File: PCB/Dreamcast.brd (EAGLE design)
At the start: 58.5 x 61 mm, 17 parts

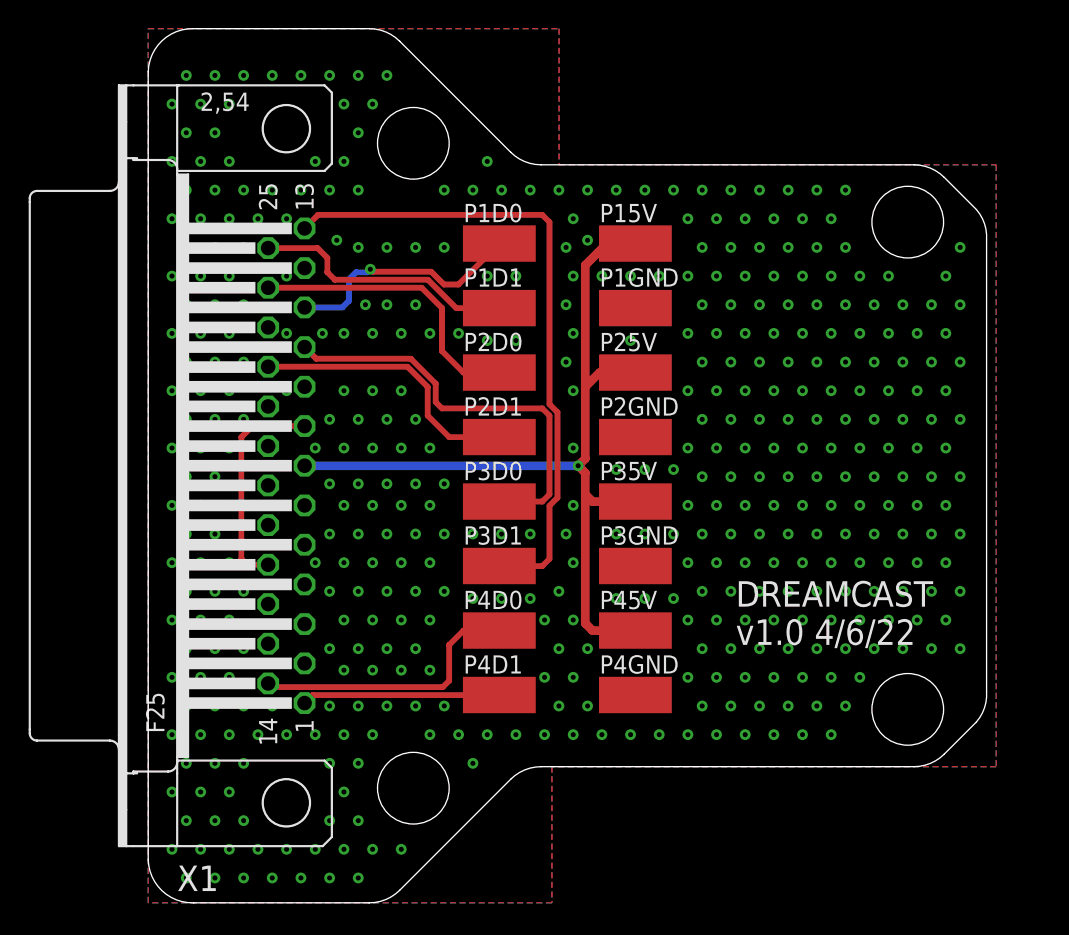
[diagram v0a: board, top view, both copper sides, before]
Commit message: Updates from Issues 42/43/18
Closed Issues 42 and 43 as Sega Genesis and PSX have been successfully tested and functional.

Updated Dreamcast PCB per comment in Issue 18 - Reversed P1-P4 pads to match housing

Updated Project Status to reflect #42 and #43 Complete
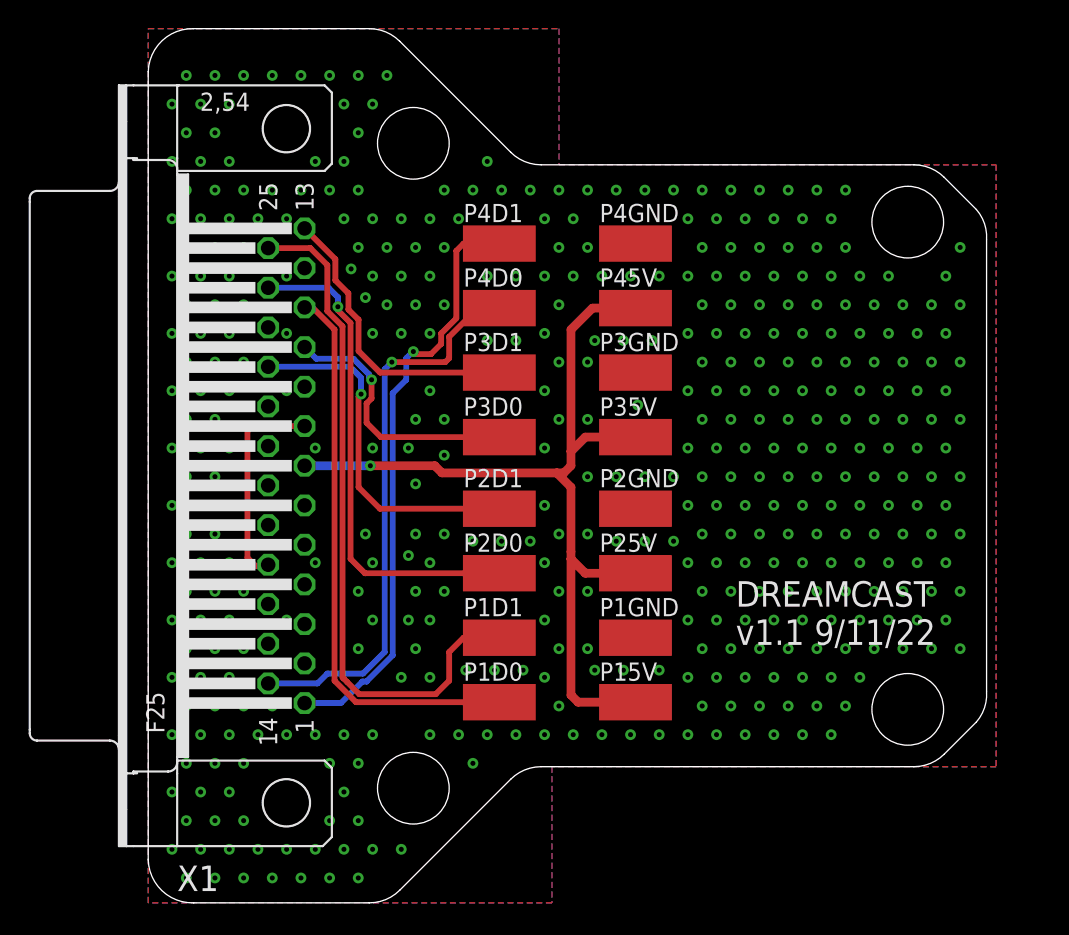
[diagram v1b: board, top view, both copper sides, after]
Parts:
- moved P15V 32.0 mm to (34.0, 14.0)
- moved P1D0 32.0 mm to (24.5, 14.0)
- moved P4D1 31.5 mm to (24.5, 46.0)
- moved P4GND 31.5 mm to (34.0, 46.0)
- moved P1D1 23.0 mm to (24.5, 18.5)
- moved P1GND 23.0 mm to (34.0, 18.5)
- moved P45V 22.5 mm to (34.0, 41.5)
- moved P4D0 22.5 mm to (24.5, 41.5)
- moved P25V 14.0 mm to (34.0, 23.0)
- moved P2D0 14.0 mm to (24.5, 23.0)
- moved P3D1 13.5 mm to (24.5, 37.0)
- moved P3GND 13.5 mm to (34.0, 37.0)
- moved P2D1 5.00 mm to (24.5, 27.5)
- moved P2GND 5.00 mm to (34.0, 27.5)
- moved P35V 4.50 mm to (34.0, 32.5)
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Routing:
- net IO22: track 18.5 -> 48.1 mm
- net IO27: track 13.8 -> 41.8 mm, vias 0 -> 1
- net IO23: track 45.4 -> 20.6 mm
- net IO21: track 17.2 -> 39.4 mm, vias 1 -> 0
- net IO26: track 19.3 -> 39.4 mm, vias 0 -> 1
- net IO3: track 20.3 -> 34.6 mm, vias 0 -> 1
- net IO18: track 29.0 -> 18.6 mm, vias 0 -> 1
- net IO5: track 19.3 -> 25.0 mm, vias 0 -> 1
- net VIN: track 60.0 -> 64.1 mm
- net JMPR: track 15.3 -> 14.7 mm
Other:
- board text added: "DREAMCAST v1.1 9/11/22"
- board text removed: "DREAMCAST v1.0 4/6/22"

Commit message: Added exposed GND plane at DB25 anchors
All PCBs have been update to have exposed GND plane pads for the DB25 anchor points.

This resolves Issue 54
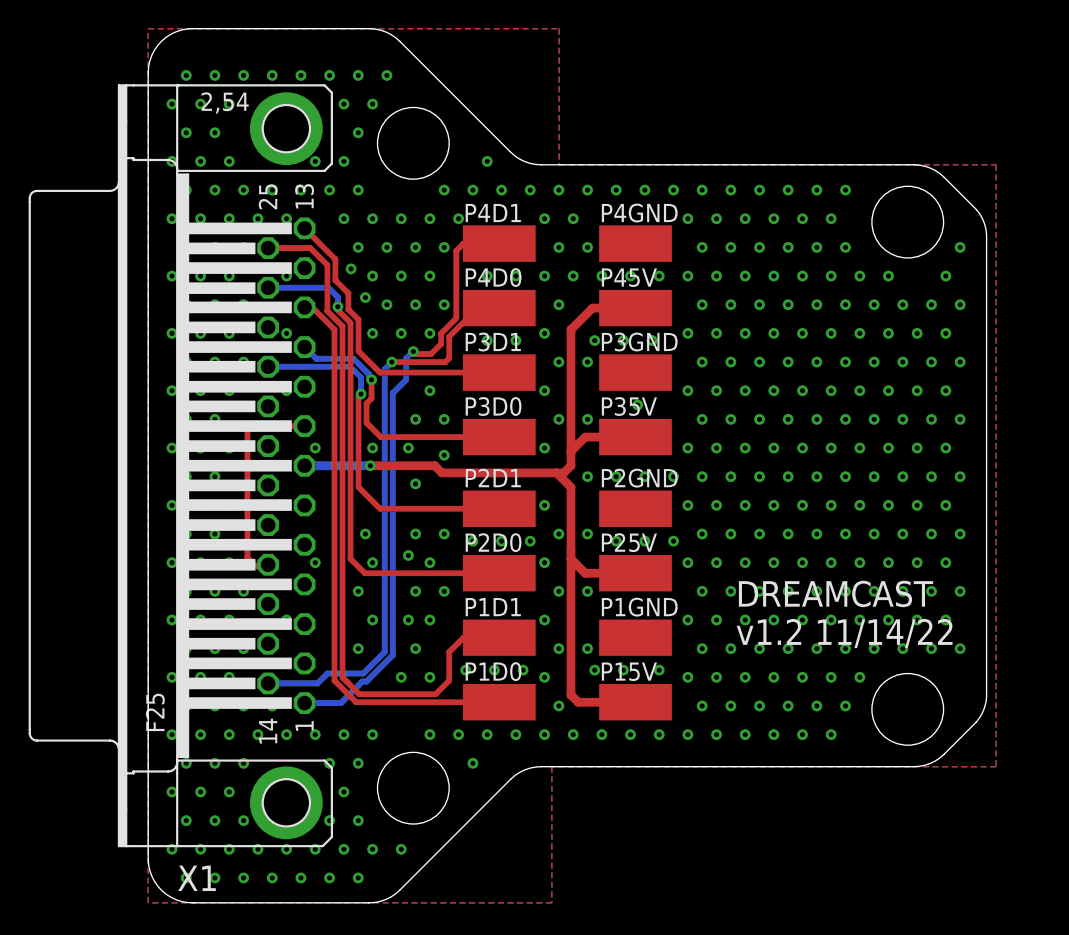
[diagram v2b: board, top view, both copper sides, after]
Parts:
- X1: device SparkFun-Retired:F25H -> SparkFun-Retired:F25HP
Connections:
- net GND: now also X1.GND1, X1.GND2
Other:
- board text added: "DREAMCAST v1.2 11/14/22"
- board text removed: "DREAMCAST v1.1 9/11/22"
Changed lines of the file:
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@@
 <hole x="18.5" y="8" drill="5"/>
 <text x="41" y="18" size="1.778" layer="21">DREAMCAST
-v1.1 9/11/22</text>
+v1.2 11/14/22</text>
 </plain>
 <attributes>
@@
 <attribute name="VALUE" x="34" y="46" size="0.0254" layer="27" rot="R270"/>
 </element>
-<element name="X1" library="SparkFun-Retired" package="F25H" value="" x="9.64" y="30.5" smashed="yes" rot="R90">
+<element name="X1" library="SparkFun-Retired" package="F25HP" value="" x="9.64" y="30.5" smashed="yes" rot="R90">
 <attribute name="NAME" x="4.919" y="2.6" size="1.778" layer="25" ratio="10" rot="R180"/>
 <attribute name="VALUE" x="-4.33" y="22.118" size="1.778" layer="27" ratio="10" rot="R90"/>
@@
 <signals>
 <signal name="GND">
-<contactref element="X1" pad="2"/>
-<contactref element="X1" pad="3"/>
-<contactref element="X1" pad="4"/>
-<contactref element="X1" pad="5"/>
-<contactref element="X1" pad="15"/>
-<contactref element="X1" pad="16"/>
-<contactref element="X1" pad="6"/>
-<contactref element="X1" pad="9"/>
 <contactref element="P1GND" pad="1"/>
 <contactref element="P4GND" pad="1"/>
@@
 <vertex x="28.17" y="0"/>
 </polygon>
-<contactref element="X1" pad="23"/>
 <via x="2.6568" y="1.735840625" extent="1-16" drill="0.35"/>
 <via x="1.6568" y="3.735840625" extent="1-16" drill="0.35"/>
@@
 <via x="55.6568" y="43.735840625" extent="1-16" drill="0.35"/>
 <via x="56.6568" y="45.735840625" extent="1-16" drill="0.35"/>
+<contactref element="X1" pad="2"/>
+<contactref element="X1" pad="3"/>
+<contactref element="X1" pad="4"/>
+<contactref element="X1" pad="5"/>
+<contactref element="X1" pad="15"/>
+<contactref element="X1" pad="16"/>
+<contactref element="X1" pad="6"/>
+<contactref element="X1" pad="9"/>
+<contactref element="X1" pad="23"/>
+<contactref element="X1" pad="GND1"/>
+<contactref element="X1" pad="GND2"/>
 </signal>
 <signal name="IO5">
